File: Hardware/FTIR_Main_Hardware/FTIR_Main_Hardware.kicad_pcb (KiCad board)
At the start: 2 copper layers, 85.9 x 53.1 mm, 46 parts, among them J1 RJ45_LED_Shielded, Q1 IRF7606PBF, Q2 BSS138, Q4 IRF7606PBF, Q6 BSS138, U2 D36V28F7, U3 OKI, U4 TMC2208_Breakout, U6 Teensy4.1_DEV-16771

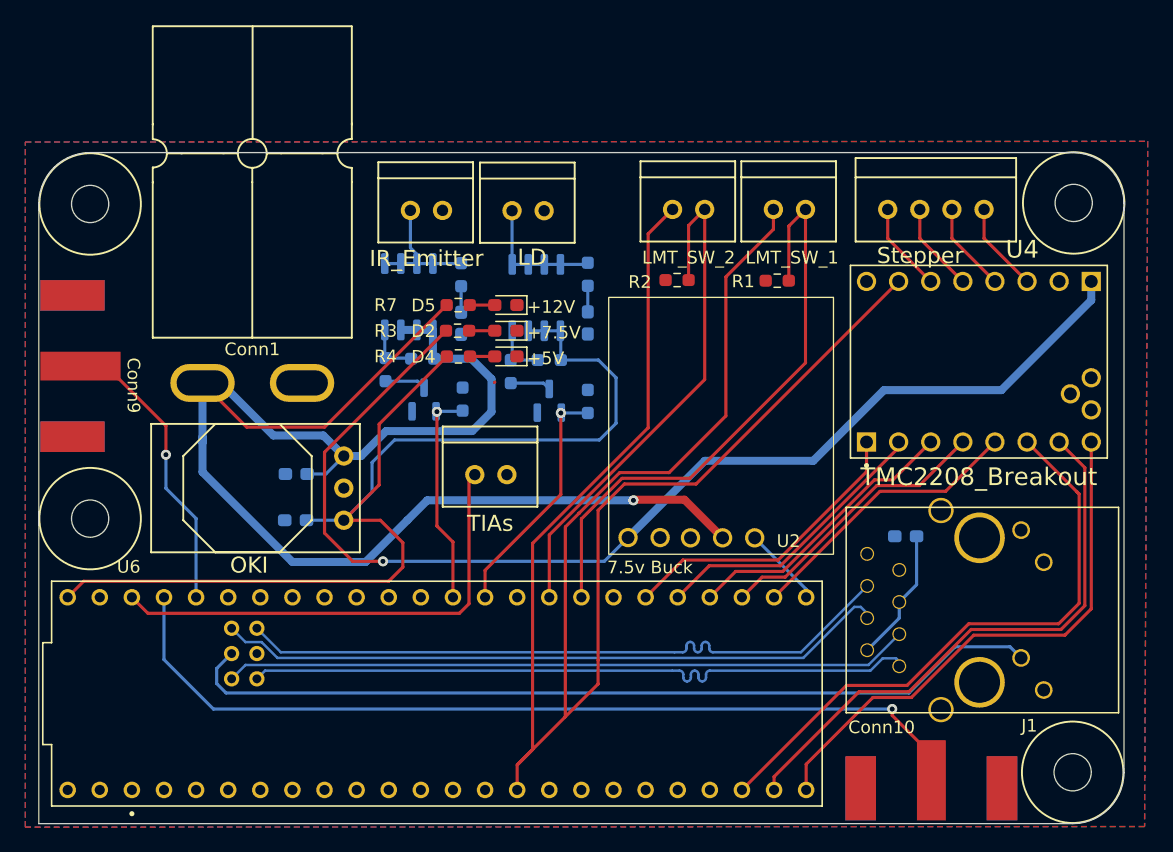
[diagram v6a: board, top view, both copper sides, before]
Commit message: Fixed power traces
Preventing reflections
Stopping 12v traces from going through vias/pads
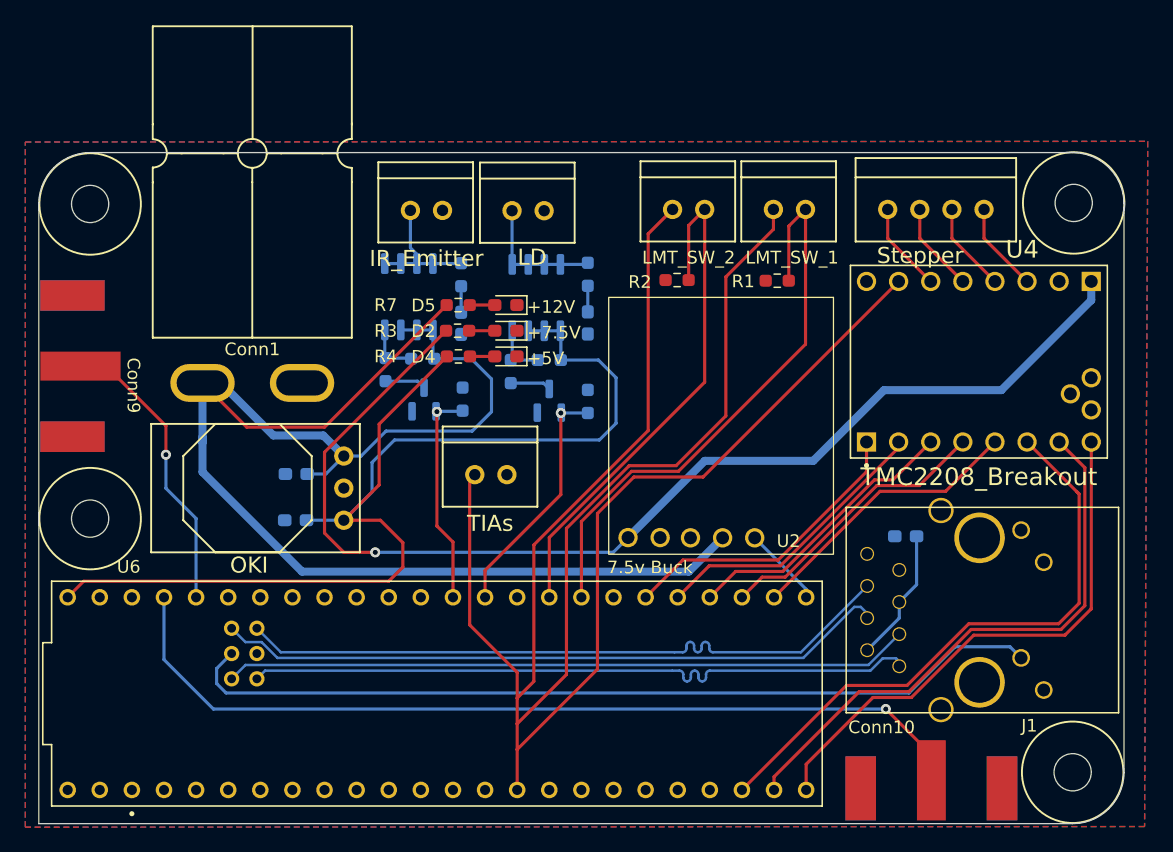
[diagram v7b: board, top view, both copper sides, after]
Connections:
- Conn1 pad 2: (no net) -> +12V
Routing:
- net +3V3: track 192.7 -> 174.4 mm
- net +12V: track 122.9 -> 121.0 mm, vias 1 -> 0
- net Net-(U6-A16): track 47.4 -> 46.4 mm
- net +7.5V: track 91.6 -> 91.0 mm

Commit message: Fixes to main board
See layout review
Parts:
- moved D4 3.31 mm to (136.0, 77.7)
- moved R4 3.31 mm to (132.2, 77.7)
- moved D2 2.53 mm to (136.0, 74.7)
- moved R3 2.53 mm to (132.2, 74.7)
- moved D5 2.07 mm to (135.9, 71.7)
- moved R7 2.07 mm to (132.1, 71.7)
- moved Conn3 0.66 mm to (135.4, 84.9)
- moved Conn4 0.25 mm to (168.0, 63.6)
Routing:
- net +5V: track 93.6 -> 89.8 mm
- net +7.5V: track 91.0 -> 87.8 mm
- net +12V: track 121.0 -> 118.4 mm
- net +3V3: track 174.4 -> 173.8 mm
